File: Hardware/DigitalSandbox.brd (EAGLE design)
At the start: 109.2 x 76.2 mm, 82 parts, among them J1 AVR_SPI_PRG_6NS, Q1 MOSFET-N, Q2 MOSFET-P, Q3 MMBT2222A, Q4 MMBT2222A, Q5 MMBT2222A, U1 MCP73831, U10 LIGHTSENSORALS, U2 ATMEGA328, U3 C2031N-1A2-B10K-GP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

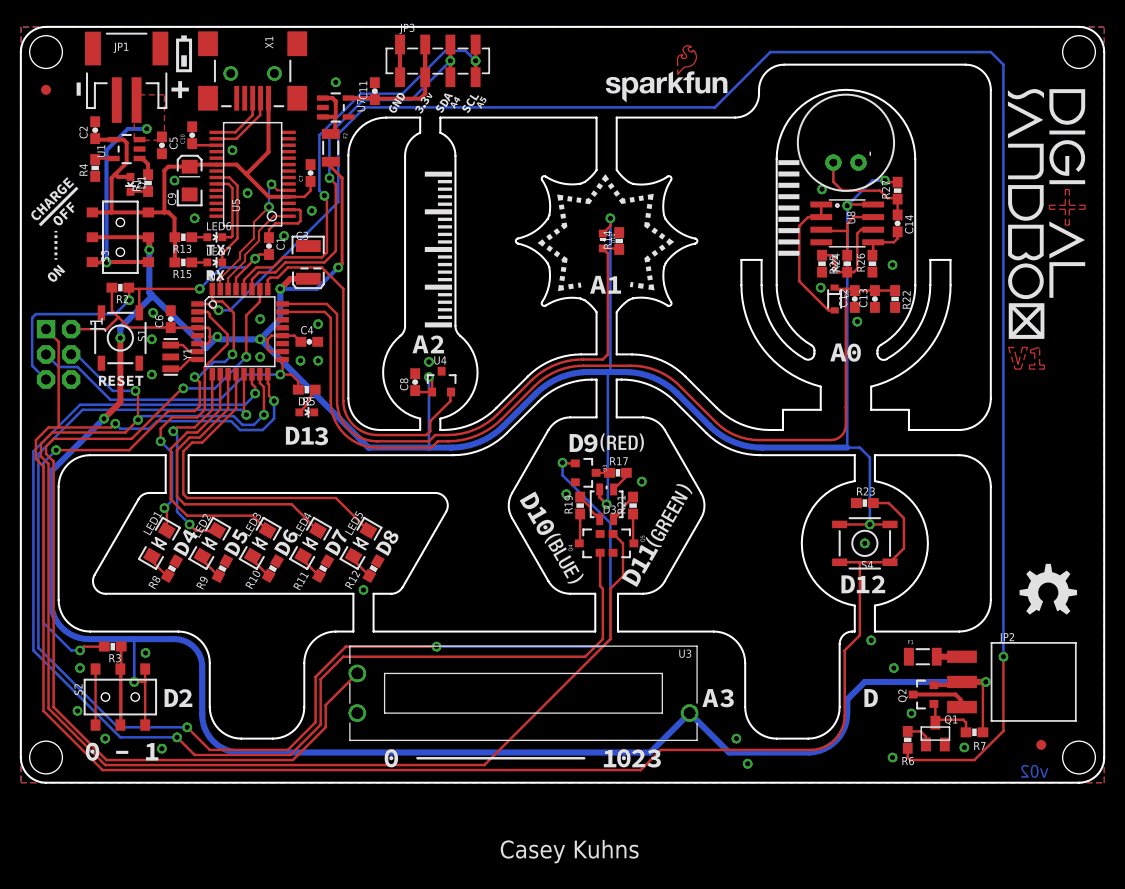
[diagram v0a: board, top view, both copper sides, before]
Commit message: corrected silk and moved vias to prevent ground plane breaks. Touched up layout of schematic to add tags and remove confusing junctions
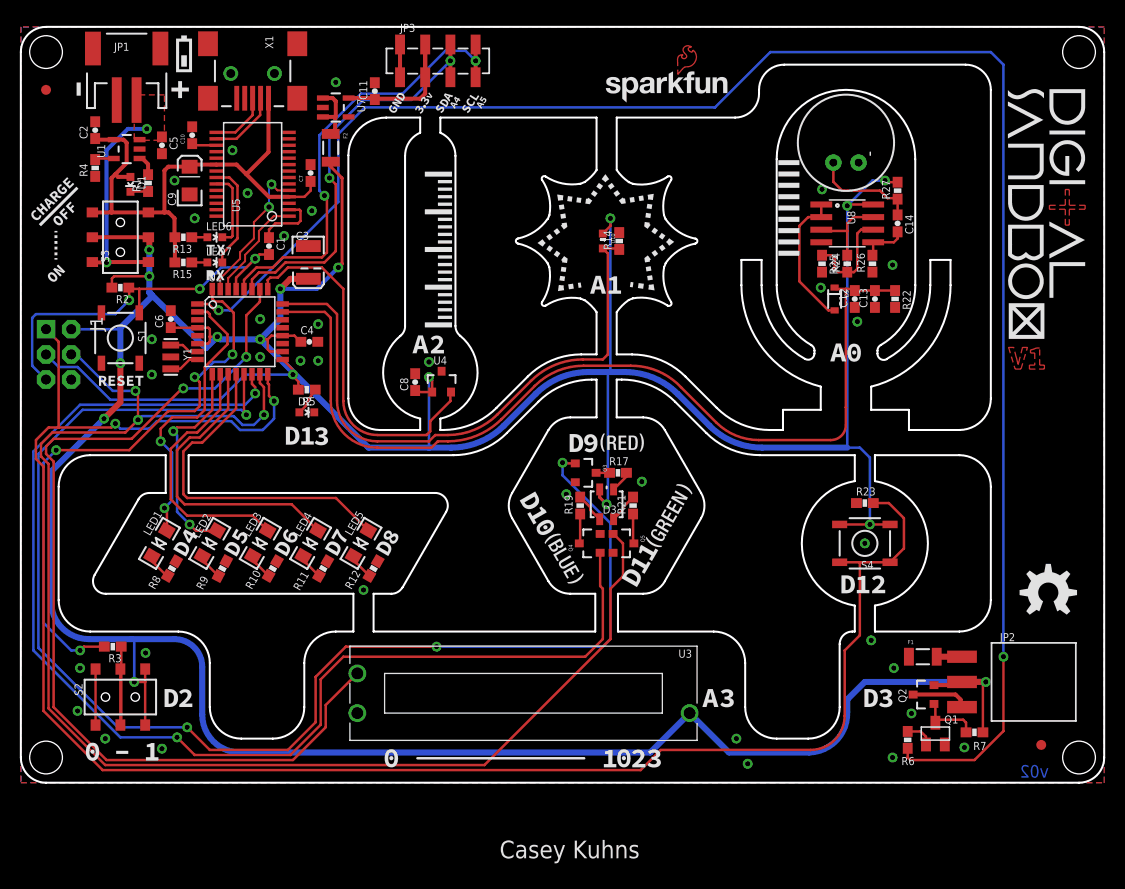
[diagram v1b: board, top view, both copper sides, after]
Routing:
- net VCC: track 407.9 -> 403.5 mm, vias 15 -> 16
- net GND: vias 36 -> 35

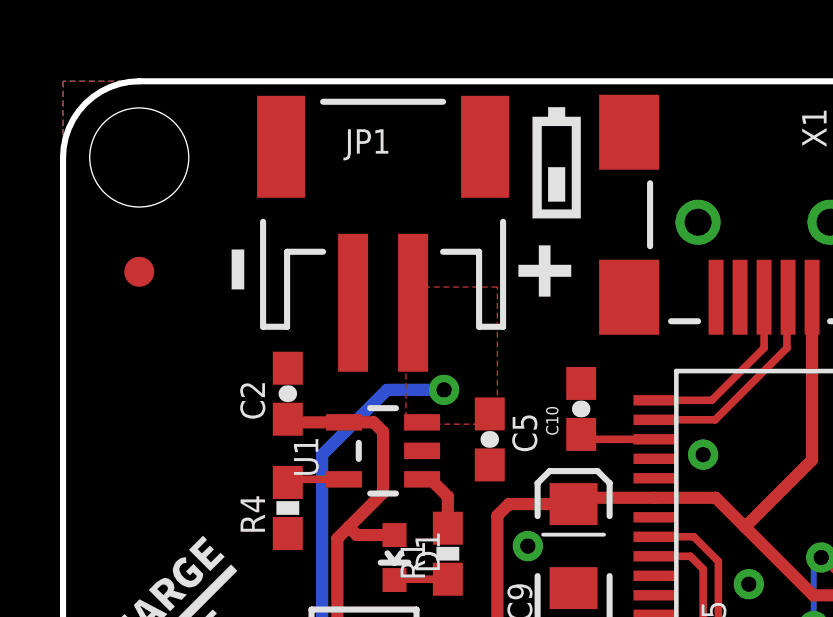
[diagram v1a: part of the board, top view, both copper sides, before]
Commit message: Added testpoints for battery charger
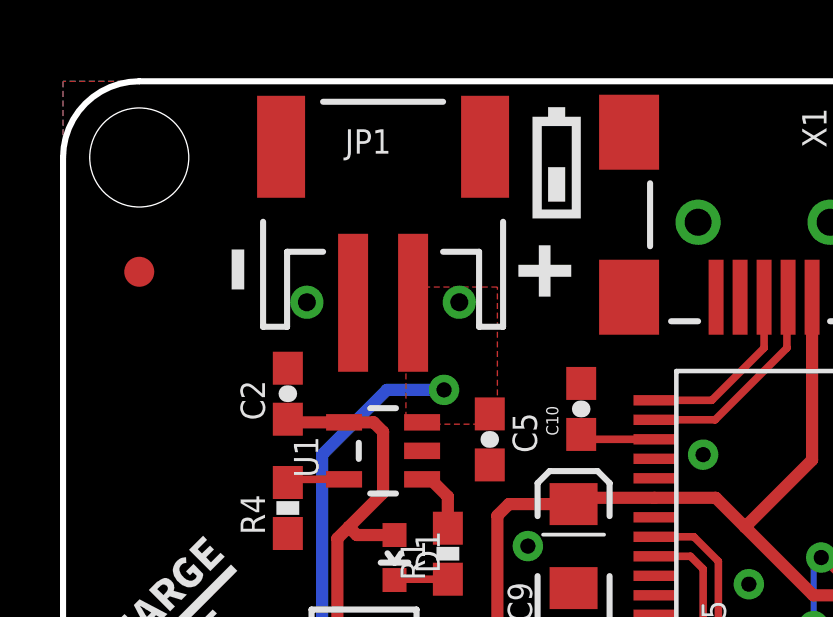
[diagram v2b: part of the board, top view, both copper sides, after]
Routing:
- net VBATT: vias 2 -> 3
- net GND: vias 35 -> 36
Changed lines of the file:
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@@
 <via x="62.611" y="30.353" extent="1-16" drill="0.508"/>
 <contactref element="J1" pad="6"/>
+<via x="8.128" y="68.834" extent="1-16" drill="0.6"/>
 </signal>
 <signal name="VCC" class="1">
@@
 <wire x1="12.858" y1="52.491" x2="8.676" y2="52.491" width="0.4064" layer="1"/>
 <wire x1="8.676" y1="52.491" x2="8.636" y2="52.451" width="0.4064" layer="1"/>
+<via x="13.208" y="68.834" extent="1-16" drill="0.6"/>
 </signal>
 <signal name="N$33">

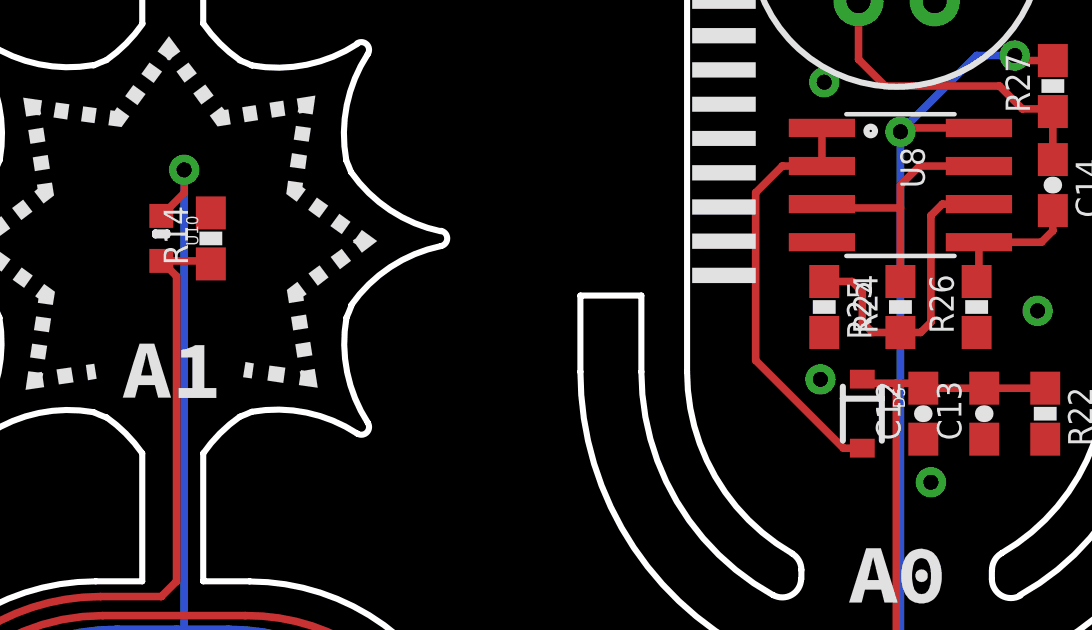
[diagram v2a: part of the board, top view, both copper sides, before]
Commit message: modified Transistor names to reflect BOM I will add a new part the the LIB soon
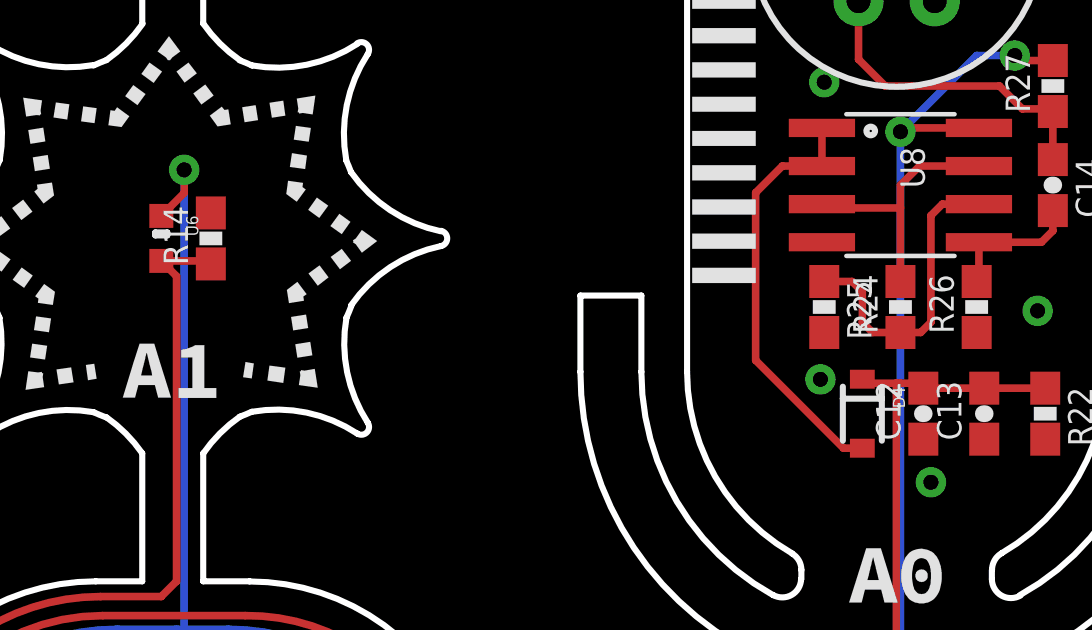
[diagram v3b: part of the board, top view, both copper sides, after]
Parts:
- Q3, Q4, Q5: value MMBT2222A -> TRANS-11480
- renumbered D5 to D4, U10 to U6
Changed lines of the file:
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@@
 <element name="F1" library="SparkFun-PowerIC" package="PTC-1206" value="PTCSMD" x="90.932" y="12.7"/>
 <element name="F2" library="SparkFun-PowerIC" package="PTC-1206" value="PTCSMD" x="31.242" y="64.008" rot="R270"/>
-<element name="Q3" library="SparkFun-DiscreteSemi" package="SOT23-3" value="MMBT2222A" x="56.896" y="31.242" rot="R270">
+<element name="Q3" library="SparkFun-DiscreteSemi" package="SOT23-3" value="TRANS-11480" x="56.896" y="31.242" rot="R270">
 <attribute name="PROD_ID" value="TRANS-08049" x="56.896" y="31.242" size="1.778" layer="27" rot="R270" display="off"/>
 </element>
-<element name="Q4" library="SparkFun-DiscreteSemi" package="SOT23-3" value="MMBT2222A" x="57.404" y="24.13" rot="R90">
+<element name="Q4" library="SparkFun-DiscreteSemi" package="SOT23-3" value="TRANS-11480" x="57.404" y="24.13" rot="R90">
 <attribute name="PROD_ID" value="TRANS-08049" x="57.404" y="24.13" size="1.778" layer="27" rot="R90" display="off"/>
 </element>
-<element name="Q5" library="SparkFun-DiscreteSemi" package="SOT23-3" value="MMBT2222A" x="60.706" y="24.13" rot="R270">
+<element name="Q5" library="SparkFun-DiscreteSemi" package="SOT23-3" value="TRANS-11480" x="60.706" y="24.13" rot="R270">
 <attribute name="PROD_ID" value="TRANS-08049" x="60.706" y="24.13" size="1.778" layer="27" rot="R270" display="off"/>
 </element>
-<element name="U10" library="SparkFun-Sensors" package="ALS-PT19" value="LIGHTSENSORALS" x="58.674" y="54.61" rot="R270">
+<element name="U6" library="SparkFun-Sensors" package="ALS-PT19" value="LIGHTSENSORALS" x="58.674" y="54.61" rot="R270">
 <attribute name="PROD_ID" value="IC-11836" x="58.674" y="54.61" size="1.778" layer="27" rot="R270" display="off"/>
 </element>
-<element name="D5" library="SparkFun-DiscreteSemi" package="SOD-323" value="" x="82.042" y="48.768" rot="R270">
+<element name="D4" library="SparkFun-DiscreteSemi" package="SOD-323" value="" x="82.042" y="48.768" rot="R270">
 <attribute name="PROD_ID" value="DIO-09646" x="82.042" y="48.768" size="0.8128" layer="27" font="vector" ratio="15" rot="R270" display="off"/>
 </element>
@@
 <wire x1="22.098" y1="3.048" x2="63.454" y2="3.048" width="0.6096" layer="16"/>
 <wire x1="63.454" y1="3.048" x2="67.423" y2="7.017" width="0.6096" layer="16"/>
-<contactref element="U10" pad="C"/>
+<contactref element="U6" pad="C"/>
 <wire x1="59.436" y1="56.896" x2="59.436" y2="56.122" width="0.254" layer="1"/>
 <wire x1="59.436" y1="56.122" x2="58.674" y2="55.36" width="0.254" layer="1"/>
@@
 <wire x1="83.176" y1="36.059" x2="81.661" y2="34.544" width="0.254" layer="1" curve="-90"/>
 <wire x1="81.661" y1="34.544" x2="74.396471875" y2="34.544" width="0.254" layer="1"/>
-<contactref element="D5" pad="1"/>
+<contactref element="D4" pad="1"/>
 <wire x1="83.908" y1="49.784" x2="83.312" y2="49.784" width="0.254" layer="1"/>
 <wire x1="83.176" y1="49.784" x2="82.176" y2="49.784" width="0.254" layer="1"/>
@@
 <wire x1="58.674" y1="42.672" x2="59.182" y2="43.18" width="0.254" layer="1"/>
 <wire x1="59.182" y1="43.18" x2="59.182" y2="53.352" width="0.254" layer="1"/>
-<contactref element="U10" pad="E"/>
+<contactref element="U6" pad="E"/>
 <wire x1="59.182" y1="53.352" x2="58.674" y2="53.86" width="0.254" layer="1"/>
 <wire x1="58.674" y1="53.86" x2="60.225" y2="53.86" width="0.254" layer="1"/>
@@
 <wire x1="80.6958" y1="57.023" x2="80.6958" y2="58.293" width="0.254" layer="1"/>
 <wire x1="80.6958" y1="57.023" x2="79.375" y2="57.023" width="0.254" layer="1"/>
-<contactref element="D5" pad="2"/>
+<contactref element="D4" pad="2"/>
 <wire x1="79.375" y1="57.023" x2="78.486" y2="56.134" width="0.254" layer="1"/>
 <wire x1="78.486" y1="56.134" x2="78.486" y2="50.546" width="0.254" layer="1"/>
